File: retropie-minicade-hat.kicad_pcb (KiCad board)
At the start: 4 copper layers, 65 x 32.7 mm, 17 parts, among them J1 40HAT, J2 Screw_Terminal_01x02, J3 Conn_02x02_Odd_Even, J4 Conn_02x02_Odd_Even, J5 Conn_01x08_Male, J6 Conn_01x08_Male, J7 Conn_01x03_Male, J8 Conn_02x03_Odd_Even, Q1 DMG2305UX, Q2 MMDT5401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

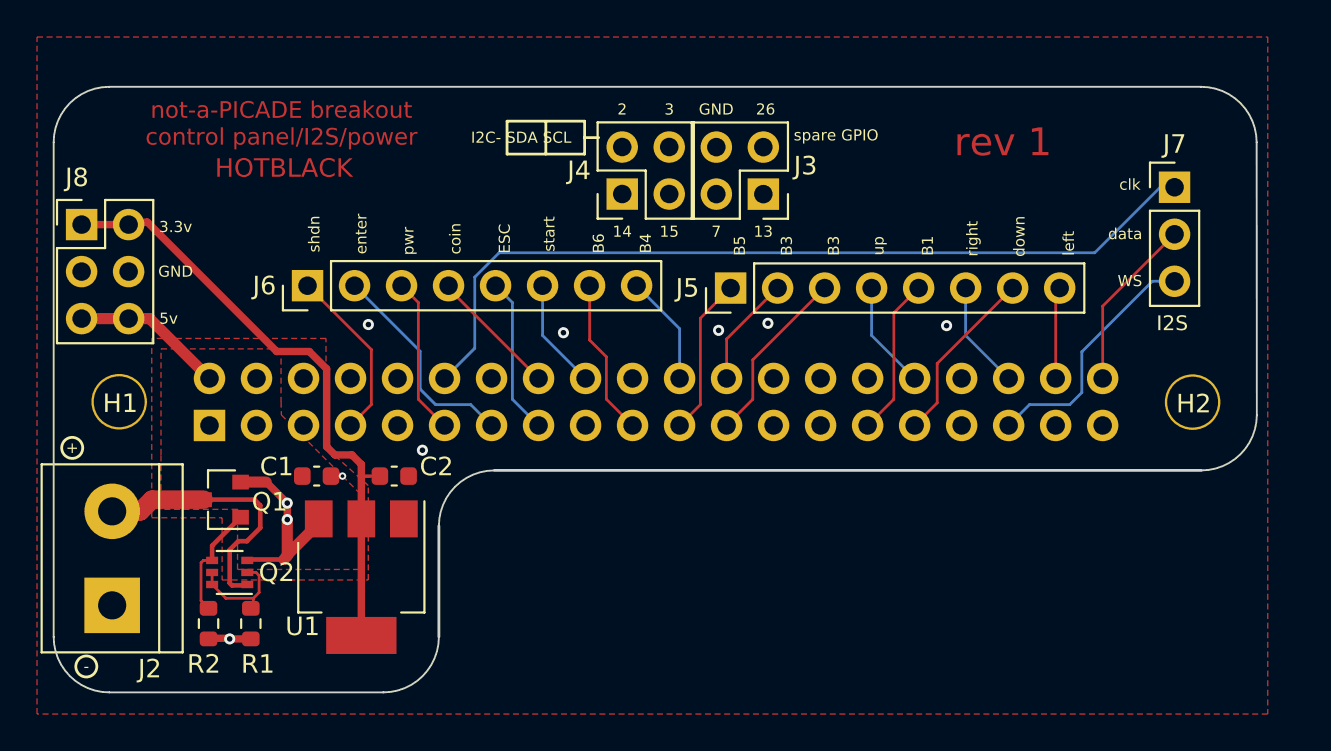
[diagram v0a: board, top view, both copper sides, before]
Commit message: tweaks to pin order to rationalize trace routes
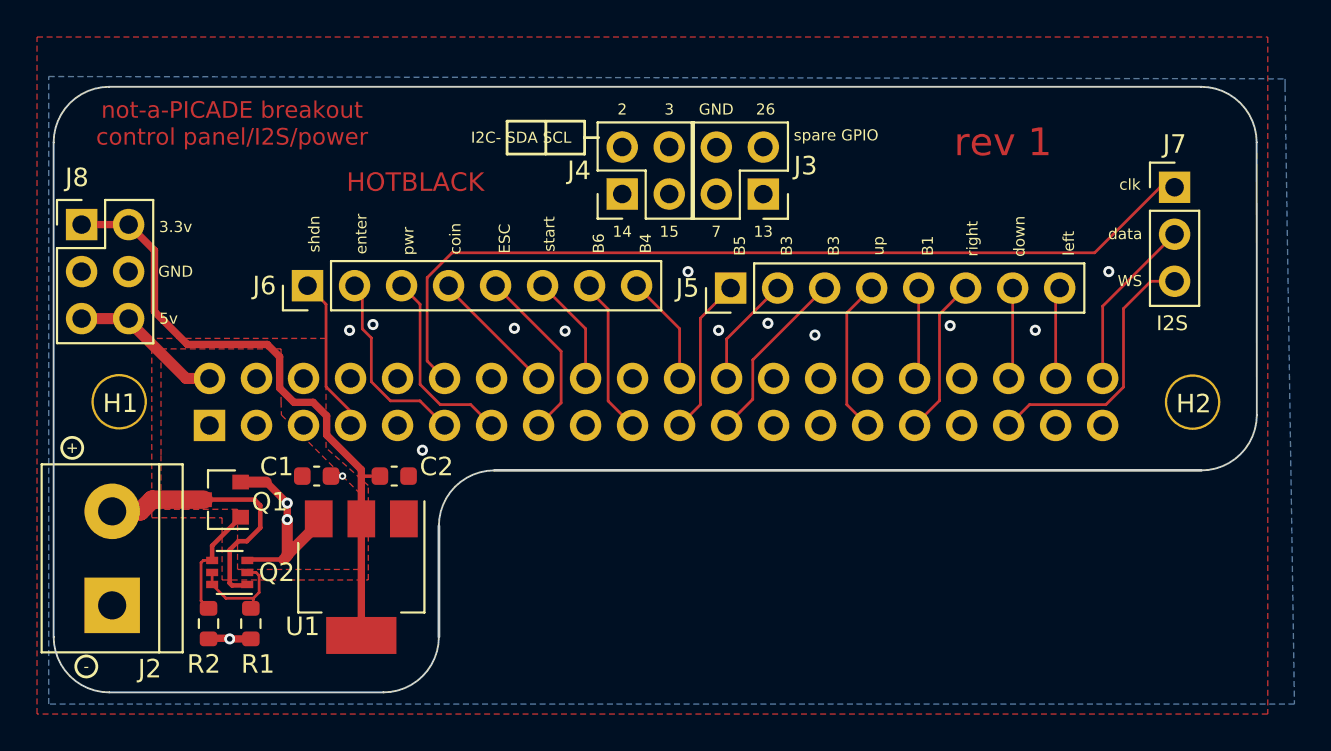
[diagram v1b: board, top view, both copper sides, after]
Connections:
- J5 pad 4: /JOY_UP -> /BUTT_1
- J5 pad 5: /BUTT_1 -> /JOY_UP
- J5 pad 6: /JOY_RIGHT -> /JOY_DOWN
- J5 pad 7: /JOY_DOWN -> /JOY_RIGHT
- J6 pad 2: /ENTER -> /PWR_BUTT
- J6 pad 3: /PWR_BUTT -> /ENTER
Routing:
- net /I2S_CLOCK: track 46.0 -> 48.2 mm
- net /PWR_BUTT: track 8.51 -> 10.5 mm
- net /SP_GPIO_2: track 27.5 -> 28.8 mm
- net /ENTER: track 11.7 -> 10.5 mm
- net /I2S_WS: track 13.5 -> 14.7 mm
- net /JOY_DOWN: track 9.62 -> 8.57 mm
- net /ESC: track 8.51 -> 9.52 mm
- net /SHUTDOWN: track 9.44 -> 8.51 mm
- net /P3V3_HAT: track 34.0 -> 34.9 mm
- net /JOY_UP: track 5.85 -> 4.97 mm
- net /JOY_RIGHT: track 5.85 -> 4.97 mm
- net GND: vias 8 -> 14
- added copper zone on B.Cu, net GND
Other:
- board text added: "Hotblack Desiato: {dblquote}...{dblquote} Minder: {dblquote}He's spending a year dead for tax purposes{dblquote}"
- board text removed: "Hotblack Desiato: {dblquote}{dblquote} Hotblack's Minder: {dblquote}He's spending a year dead for tax purposes{dblquote}"

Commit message: re-did the silkscreen labels
pins and traces were changed but not the pin labels. fixed
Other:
- board text added: "B2"
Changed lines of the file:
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@@
     (effects (font (size 0.6 0.6) (thickness 0.09)))
   )
-  (gr_text "up" (at 123.063 55.88 90) (layer "F.SilkS")
+  (gr_text "up" (at 125.73 56.007 90) (layer "F.SilkS")
     (effects (font (size 0.6 0.6) (thickness 0.09)))
   )
@@
     (effects (font (size 0.6 0.6) (thickness 0.09)))
   )
-  (gr_text "B3" (at 120.65 55.88 90) (layer "F.SilkS")
+  (gr_text "B2" (at 120.65 55.88 90) (layer "F.SilkS")
     (effects (font (size 0.6 0.6) (thickness 0.09)))
   )
@@
     (effects (font (size 0.6 0.6) (thickness 0.09)))
   )
-  (gr_text "B1" (at 125.73 55.88 90) (layer "F.SilkS")
+  (gr_text "B1" (at 123.063 56.007 90) (layer "F.SilkS")
     (effects (font (size 0.6 0.6) (thickness 0.09)))
   )
@@
     (effects (font (size 0.8 0.8) (thickness 0.1)))
   )
-  (gr_text "enter" (at 95.123 55.245 90) (layer "F.SilkS")
+  (gr_text "enter" (at 97.79 55.245 90) (layer "F.SilkS")
     (effects (font (size 0.6 0.6) (thickness 0.09)))
   )
@@
     (effects (font (size 0.6 0.6) (thickness 0.09)))
   )
-  (gr_text "down" (at 130.683 55.372 90) (layer "F.SilkS")
+  (gr_text "down" (at 128.143 55.372 90) (layer "F.SilkS")
     (effects (font (size 0.6 0.6) (thickness 0.09)))
   )
@@
     (effects (font (size 0.6 0.6) (thickness 0.09)))
   )
-  (gr_text "pwr" (at 97.663 55.626 90) (layer "F.SilkS")
+  (gr_text "pwr" (at 95.123 55.626 90) (layer "F.SilkS")
     (effects (font (size 0.6 0.6) (thickness 0.09)))
   )
@@
     (effects (font (size 0.6 0.6) (thickness 0.09)))
   )
-  (gr_text "right" (at 128.143 55.499 90) (layer "F.SilkS")
+  (gr_text "right" (at 130.683 55.499 90) (layer "F.SilkS")
     (effects (font (size 0.6 0.6) (thickness 0.09)))
   )
